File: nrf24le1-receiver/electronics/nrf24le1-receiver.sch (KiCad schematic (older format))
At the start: 19 parts, among them K1 CONN_3, K2 CONN_3, K3 CONN_3, K4 CONN_3, P1 CONN_1, P2 CONN_1, P3 CONN_1, SW1 BIND, U1 MCP1703, U2 NRF24LE1-MODULE-15X21

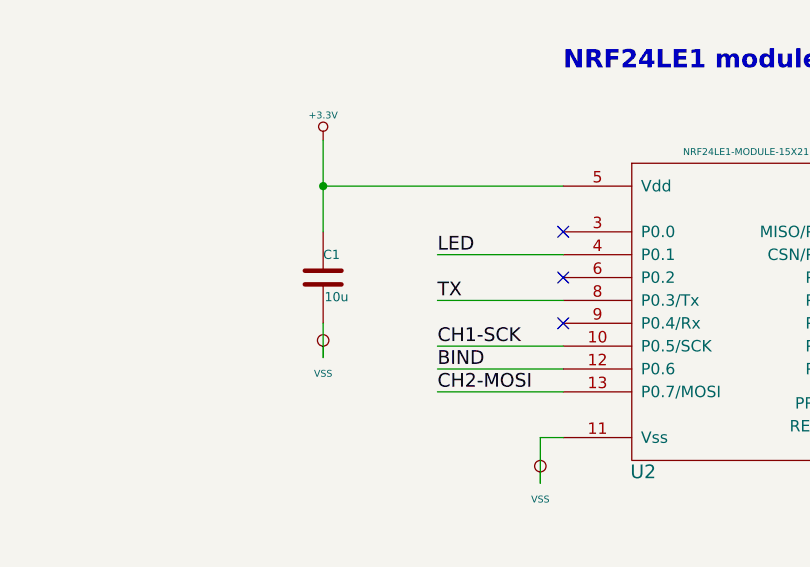
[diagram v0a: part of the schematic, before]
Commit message: Add 2x 47uF 0805 tantalum bypass cap to combat brown-outs
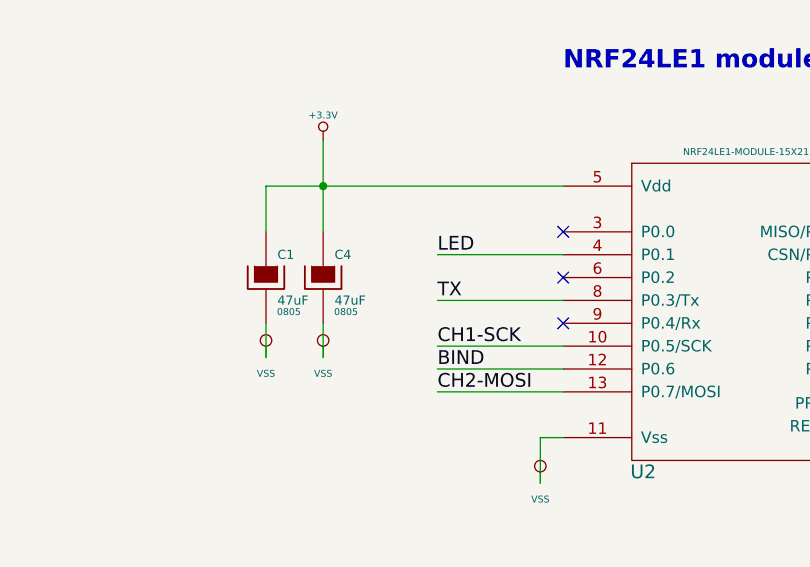
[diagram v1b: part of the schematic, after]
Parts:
- removed C1: 10u, ~, symbol C
- added C1, C4: 47uF, 0805, symbol CP
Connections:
- net +3.3V: now also C1.1, C4.1
- net VSS: now also C1.2, C4.2
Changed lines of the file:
@@
 Sheet 1 1
 Title ""
-Date "30 nov 2014"
-Rev ""
+Date "5 jan 2015"
+Rev "2"
 Comp ""
 Comment1 ""
@@
 F 3 "~" H 1700 6350 60  0000 C CNN
 	1    1700 6350
-	1    0    0    -1
-$EndComp
-$Comp
-L C C1
-U 1 1 54792183
-P 2300 2600
-F 0 "C1" H 2300 2700 40  0000 L CNN
-F 1 "10u" H 2306 2515 40  0000 L CNN
-F 2 "~" H 2338 2450 30  0000 C CNN
-F 3 "~" H 2300 2600 60  0000 C CNN
-	1    2300 2600
 	1    0    0    -1
 $EndComp
@@
 	9300 3000 9700 3000
 Wire Wire Line
-	3350 2200 2300 2200
+	2050 2200 3350 2200
 Wire Wire Line
 	9600 3200 9700 3200
@@
 Text Notes 8450 5100 0    80   ~ 16
 Bind button
+$Comp
+L CP C4
+U 1 1 54A9ECE7
+P 2300 2600
+F 0 "C4" H 2350 2700 40  0000 L CNN
+F 1 "47uF" H 2350 2500 40  0000 L CNN
+F 2 "0805" H 2400 2450 30  0000 C CNN
+F 3 "~" H 2300 2600 300 0000 C CNN
+	1    2300 2600
+	1    0    0    -1
+$EndComp
+$Comp
+L CP C1
+U 1 1 54A9ED05
+P 2050 2600
+F 0 "C1" H 2100 2700 40  0000 L CNN
+F 1 "47uF" H 2100 2500 40  0000 L CNN
+F 2 "0805" H 2150 2450 30  0000 C CNN
+F 3 "~" H 2050 2600 300 0000 C CNN
+	1    2050 2600
+	1    0    0    -1
+$EndComp
+$Comp
+L VSS #PWR015
+U 1 1 54A9ED8E
+P 2050 2950
+F 0 "#PWR015" H 2050 2950 30  0001 C CNN
+F 1 "VSS" H 2050 2880 30  0000 C CNN
+F 2 "" H 2050 2950 60  0000 C CNN
+F 3 "" H 2050 2950 60  0000 C CNN
+	1    2050 2950
+	1    0    0    -1
+$EndComp
+Wire Wire Line
+	2050 2800 2050 2950
+Wire Wire Line
+	2050 2400 2050 2200
 $EndSCHEMATC

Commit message: Add Gerber for revision 2 PCB
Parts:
- C1, C4: symbol CP -> CP-RESCUE-nrf24le1-receiver
- C2, C3: symbol C -> C-RESCUE-nrf24le1-receiver
- D1: symbol LED -> LED-RESCUE-nrf24le1-receiver
- R1, R2, R3, R4, R5: symbol R -> R-RESCUE-nrf24le1-receiver
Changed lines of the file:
@@
 EESchema Schematic File Version 2
+LIBS:nrf24le1-receiver-rescue
 LIBS:power
 LIBS:device
@@
 LIBS:linear
 LIBS:regul
-LIBS:special
 LIBS:microcontrollers
 LIBS:dsp
@@
 LIBS:MCP1703
 LIBS:nrf24le1-receiver-cache
-EELAYER 27 0
+EELAYER 25 0
 EELAYER END
 $Descr A4 11693 8268
@@
 $EndComp
 $Comp
-L C C3
+L C-RESCUE-nrf24le1-receiver C3
 U 1 1 5479215B
 P 4000 6400
@@
 $EndComp
 $Comp
-L C C2
+L C-RESCUE-nrf24le1-receiver C2
 U 1 1 5479216A
 P 1700 6350
@@
 $EndComp
 $Comp
-L R R2
+L R-RESCUE-nrf24le1-receiver R2
 U 1 1 5479219C
 P 9050 1650
@@
 $EndComp
 $Comp
-L R R3
+L R-RESCUE-nrf24le1-receiver R3
 U 1 1 547921A9
 P 9050 2100
@@
 $EndComp
 $Comp
-L R R4
+L R-RESCUE-nrf24le1-receiver R4
 U 1 1 547921AF
 P 9050 2550
@@
 $EndComp
 $Comp
-L R R5
+L R-RESCUE-nrf24le1-receiver R5
 U 1 1 547921B5
 P 9050 3000
@@
 $EndComp
 $Comp
-L +3.3V #PWR06
+L +3.3V-RESCUE-nrf24le1-receiver #PWR06
 U 1 1 547921F3
 P 4000 5900
@@
 $EndComp
 $Comp
-L +3.3V #PWR07
+L +3.3V-RESCUE-nrf24le1-receiver #PWR07
 U 1 1 54792200
 P 2300 2000
@@
 CH1-SCK
 $Comp
-L LED D1
+L LED-RESCUE-nrf24le1-receiver D1
 U 1 1 547928FB
 P 6300 6100
@@
 $EndComp
 $Comp
-L R R1
+L R-RESCUE-nrf24le1-receiver R1
 U 1 1 5479290A
 P 6300 5550
@@
 Bind button
 $Comp
-L CP C4
+L CP-RESCUE-nrf24le1-receiver C4
 U 1 1 54A9ECE7
 P 2300 2600
@@
 $EndComp
 $Comp
-L CP C1
+L CP-RESCUE-nrf24le1-receiver C1
 U 1 1 54A9ED05
 P 2050 2600
